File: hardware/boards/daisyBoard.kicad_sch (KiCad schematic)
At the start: 113 parts, among them IC1 TL072HIDR, IC2 TL072HIDR, IC3 TL072HIDR, IC4 TL072HIDR, J1 LEFT Pin ROW, J10 AudioJack_OUT_2, J11 AudioJack_OUT_2, J13 LEFT Pin ROW Daisy, J14 RIGHT Pin ROW DAISY, J15 Daisy Pin Breakout LEFT, J16 Daisy PIN Breakout RIGHT, J2 RIGHT Pin Row, J3 ESP32 Pin Breakout RIGHT, J4 ESP32 Pin Breakout LEFT, J6 AudioJack3, J7 AudioJack3, J8 AudioJack_IN_1, J9 AudioJack_IN_2, U1 MCP6002-xSN, U2 MCP6002-xSN, U3 MCP6002-xSN

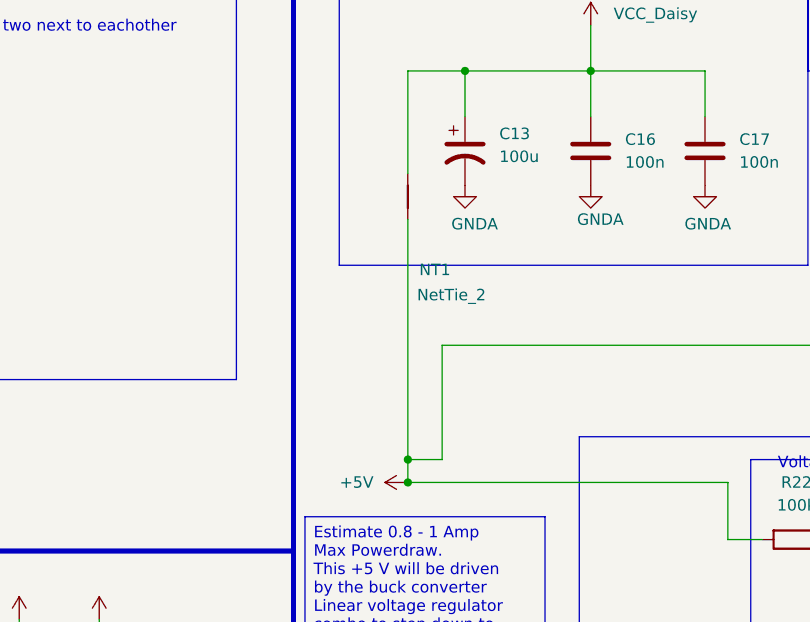
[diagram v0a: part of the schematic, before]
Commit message: moved some pads again
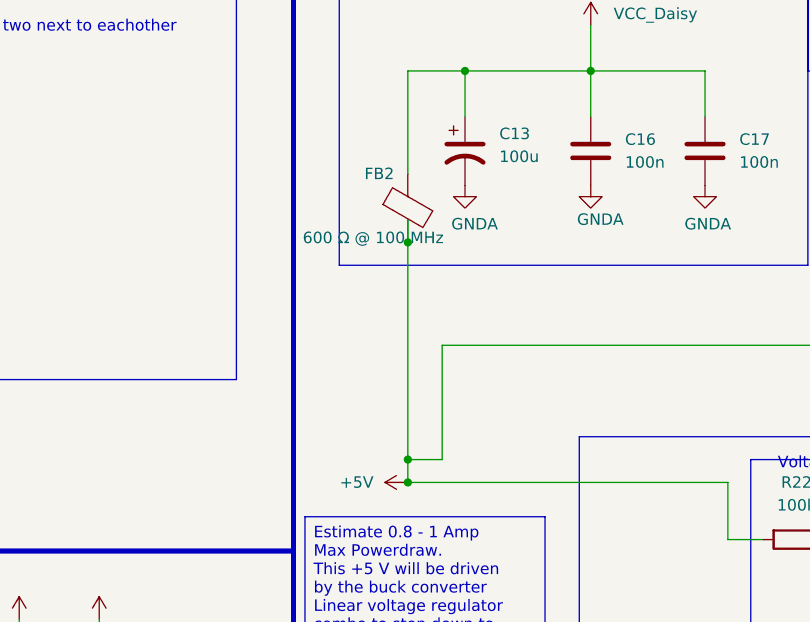
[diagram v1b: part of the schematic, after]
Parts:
- removed NT1: NetTie_2, NetTie:NetTie-2_SMD_Pad0.5mm, symbol Device:NetTie_2
- added FB2: 600 Ω @ 100 MHz, Inductor_SMD:L_0805_2012Metric, symbol Device:FerriteBead
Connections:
- net +5V: now also FB2.2
- net VCC_Daisy: now also FB2.1
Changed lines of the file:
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@@
 	)
 	(junction
+		(at 387.35 173.99)
+		(diameter 0)
+		(color 0 0 0 0)
+	)
+	(junction
 		(at 321.31 36.83)
 		(diameter 0)
@@
 	(wire
 		(pts
-			(xy 387.35 171.45) (xy 387.35 198.12)
+			(xy 387.35 171.45) (xy 387.35 173.99)
 		)
 		(stroke
@@
 	(wire
 		(pts
+			(xy 387.35 173.99) (xy 387.35 198.12)
+		)
+		(stroke
+			(width 0)
+			(type default)
+		)
+	)
+	(wire
+		(pts
 			(xy 307.34 238.76) (xy 307.34 254)
 		)
@@
 	)
 	(symbol
+		(lib_id "Device:FerriteBead")
+		(at 387.35 170.18 0)
+		(unit 1)
+		(body_style 1)
+		(exclude_from_sim no)
+		(in_bom yes)
+		(on_board yes)
+		(in_pos_files yes)
+		(dnp no)
+		(property "Reference" "FB2"
+			(at 382.524 166.37 0)
+			(show_name no)
+			(do_not_autoplace no)
+			(effects
+				(font
+					(size 1.27 1.27)
+				)
+				(justify left)
+			)
+		)
+		(property "Value" "600 Ω @ 100 MHz"
+			(at 375.666 173.482 0)
+			(show_name no)
+			(do_not_autoplace no)
+			(effects
+				(font
+					(size 1.27 1.27)
+				)
+				(justify left)
+			)
+		)
+		(property "Footprint" "Inductor_SMD:L_0805_2012Metric"
+			(at 385.572 170.18 90)
+			(hide yes)
+			(show_name no)
+			(do_not_autoplace no)
+			(effects
+				(font
+					(size 1.27 1.27)
+				)
+			)
+		)
+		(property "Datasheet" ""
+			(at 387.35 170.18 0)
+			(hide yes)
+			(show_name no)
+			(do_not_autoplace no)
+			(effects
+				(font
+					(size 1.27 1.27)
+				)
+			)
+		)
+		(property "Description" "Ferrite bead"
+			(at 387.35 170.18 0)
+			(hide yes)
+			(show_name no)
+			(do_not_autoplace no)
+			(effects
+				(font
+					(size 1.27 1.27)
+				)
+			)
+		)
+		(pin "2"
+		)
+		(pin "1"
+		)
+		(instances
+			(project "daisyBoard"
+				(path "/f52c2822-383d-4296-bc07-76547c2833aa"
+					(reference "FB2")
+					(unit 1)
+				)
+			)
+		)
+	)
+	(symbol
 		(lib_id "power:+3.3VA")
 		(at 48.26 139.7 270)
@@
 					(unit 1)
 				)
-			)
-		)
-	)
-	(symbol
-		(lib_id "Device:NetTie_2")
-		(at 387.35 168.91 90)
-		(unit 1)
-		(body_style 1)
-		(exclude_from_sim no)
-		(in_bom no)
-		(on_board yes)
-		(in_pos_files yes)
-		(dnp no)
-		(property "Reference" "NT1"
-			(at 388.62 177.038 90)
-			(show_name no)
-			(do_not_autoplace no)
-			(effects
-				(font
-					(size 1.27 1.27)
-				)
-				(justify right)
-			)
-		)
-		(property "Value" "NetTie_2"
-			(at 388.366 179.832 90)
-			(show_name no)
-			(do_not_autoplace no)
-			(effects
-				(font
-					(size 1.27 1.27)
-				)
-				(justify right)
-			)
-		)
-		(property "Footprint" "NetTie:NetTie-2_SMD_Pad0.5mm"
-			(at 387.35 168.91 0)
-			(hide yes)
-			(show_name no)
-			(do_not_autoplace no)
-			(effects
-				(font
-					(size 1.27 1.27)
-				)
-			)
-		)
-		(property "Datasheet" ""
-			(at 387.35 168.91 0)
-			(hide yes)
-			(show_name no)
-			(do_not_autoplace no)
-			(effects
-				(font
-					(size 1.27 1.27)
-				)
-			)
-		)
-		(property "Description" "Net tie, 2 pins"
-			(at 387.35 168.91 0)
-			(hide yes)
-			(show_name no)
-			(do_not_autoplace no)
-			(effects
-				(font
-					(size 1.27 1.27)
-				)
-			)
-		)
-		(pin "2"
-		)
-		(pin "1"
-		)
-		(instances
-			(project "daisyBoard"
-				(path "/f52c2822-383d-4296-bc07-76547c2833aa"
-					(reference "NT1")
-					(unit 1)
-				)

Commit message: did drc checks fix and connected flaoting pins on op amps
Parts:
- removed R24: 100R, Resistor_SMD:R_0805_2012Metric, symbol Device:R
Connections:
- net VREF: now also IC1.5 (+), IC2.5 (+), IC3.5 (+), IC4.5 (+), U3.1
- net at C15.1, C19.1, C20.1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: now also U3.5 (+)
- net at IC3.6 (-): now also IC3.7
- net at IC1.6 (-): now also IC1.7
- net at U3.6 (-): now also U3.7
- net at IC4.6 (-): now also IC4.7
- net at IC2.6 (-): now also IC2.7
- no-connect marks 25 -> 10
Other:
- note added: "Tie up floating pins"
- moved on the sheet: C29, FB2, U1C

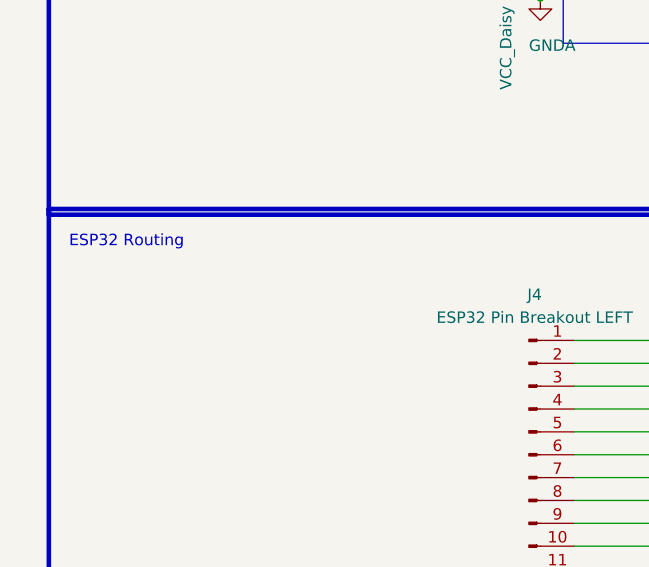
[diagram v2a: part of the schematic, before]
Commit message: updated some still in pad connections
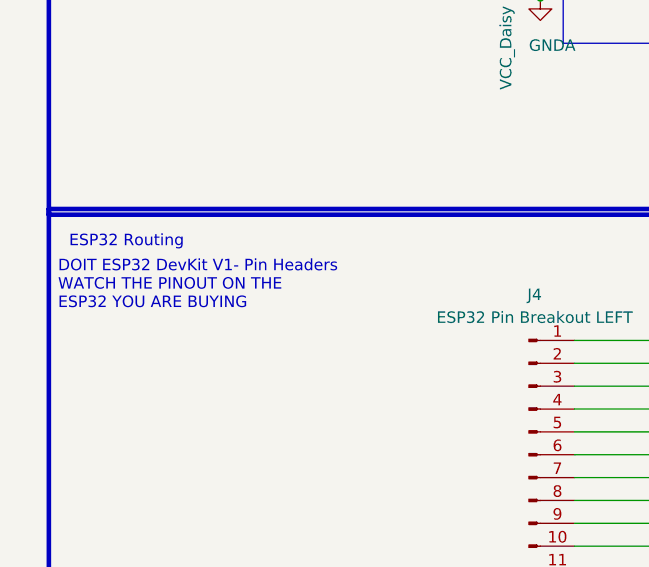
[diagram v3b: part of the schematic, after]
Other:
- note added: "DOIT ESP32 DevKit V1- Pin Headers WATCH THE PINOUT ON THE ESP32 YOU ARE BUYING"
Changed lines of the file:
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@@
+		)
+	)
+	(text "DOIT ESP32 DevKit V1- Pin Headers\nWATCH THE PINOUT ON THE \nESP32 YOU ARE BUYING"
+		(exclude_from_sim no)
+		(at 25.146 219.964 0)
+		(effects
+			(font
+				(size 1.27 1.27)
+			)
+			(justify left)
 		)
 	)

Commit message: last review and update of some things. Still need to adress VREF trace length
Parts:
- added R24: 100, Resistor_SMD:R_0805_2012Metric, symbol Device:R
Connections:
- net VREF: now also R24.2; no longer U3.1, U3.2 (-)
- new net: R24.1, U3.1, U3.2 (-)
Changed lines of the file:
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@@
 	)
 	(junction
-		(at 497.84 209.55)
-		(diameter 0)
-		(color 0 0 0 0)
-	)
-	(junction
 		(at 234.95 91.44)
 		(diameter 0)
@@
 	)
 	(junction
+		(at 497.84 209.55)
+		(diameter 0)
+		(color 0 0 0 0)
+	)
+	(junction
 		(at 252.73 91.44)
 		(diameter 0)
@@
 	(wire
 		(pts
-			(xy 497.84 209.55) (xy 505.46 209.55)
+			(xy 497.84 209.55) (xy 500.38 209.55)
 		)
 		(stroke
@@
 	(wire
 		(pts
+			(xy 508 209.55) (xy 509.27 209.55)
+		)
+		(stroke
+			(width 0)
+			(type default)
+		)
+	)
+	(wire
+		(pts
 			(xy 227.33 40.64) (xy 229.87 40.64)
 		)
@@
 	(symbol
 		(lib_id "power:+5V")
-		(at 505.46 209.55 270)
+		(at 509.27 209.55 270)
 		(unit 1)
 		(body_style 1)
@@
 		(in_pos_files yes)
 		(dnp no)
-		(fields_autoplaced yes)
 		(property "Reference" "#PWR043"
-			(at 501.65 209.55 0)
+			(at 505.46 209.55 0)
 			(hide yes)
 			(show_name no)
@@
 		)
 		(property "Value" "VREF"
-			(at 509.27 209.5499 90)
+			(at 510.032 207.01 90)
 			(show_name no)
 			(do_not_autoplace no)
@@
 		)
 		(property "Footprint" ""
-			(at 505.46 209.55 0)
+			(at 509.27 209.55 0)
 			(hide yes)
 			(show_name no)
@@
 		)
 		(property "Datasheet" ""
-			(at 505.46 209.55 0)
+			(at 509.27 209.55 0)
 			(hide yes)
 			(show_name no)
@@
 		)
 		(property "Description" "Power symbol creates a global label with name \"+5V\""
-			(at 505.46 209.55 0)
+			(at 509.27 209.55 0)
 			(hide yes)
 			(show_name no)
@@
 					(unit 1)
 				)
+			)
+		)
+	)
+	(symbol
+		(lib_id "Device:R")
+		(at 504.19 209.55 90)
+		(unit 1)
+		(body_style 1)
+		(exclude_from_sim no)
+		(in_bom yes)
+		(on_board yes)
+		(in_pos_files yes)
+		(dnp no)
+		(fields_autoplaced yes)
+		(property "Reference" "R24"
+			(at 504.19 203.2 90)
+			(show_name no)
+			(do_not_autoplace no)
+			(effects
+				(font
+					(size 1.27 1.27)
+				)
+			)
+		)
+		(property "Value" "100"
+			(at 504.19 205.74 90)
+			(show_name no)
+			(do_not_autoplace no)
+			(effects
+				(font
+					(size 1.27 1.27)
+				)
+			)
+		)
+		(property "Footprint" "Resistor_SMD:R_0805_2012Metric"
+			(at 504.19 211.328 90)
+			(hide yes)
+			(show_name no)
+			(do_not_autoplace no)
+			(effects
+				(font
+					(size 1.27 1.27)
+				)
+			)
+		)
+		(property "Datasheet" ""
+			(at 504.19 209.55 0)
+			(hide yes)
+			(show_name no)
+			(do_not_autoplace no)
+			(effects
+				(font
+					(size 1.27 1.27)
+				)
+			)
+		)
+		(property "Description" "Resistor"
+			(at 504.19 209.55 0)
+			(hide yes)
+			(show_name no)
+			(do_not_autoplace no)
+			(effects
+				(font
+					(size 1.27 1.27)
+				)
+			)
+		)
+		(pin "1"
+		)
+		(pin "2"
+		)
+		(instances
+			(project "daisyBoard"
+				(path "/f52c2822-383d-4296-bc07-76547c2833aa"
+					(reference "R24")
+					(unit 1)
+				)

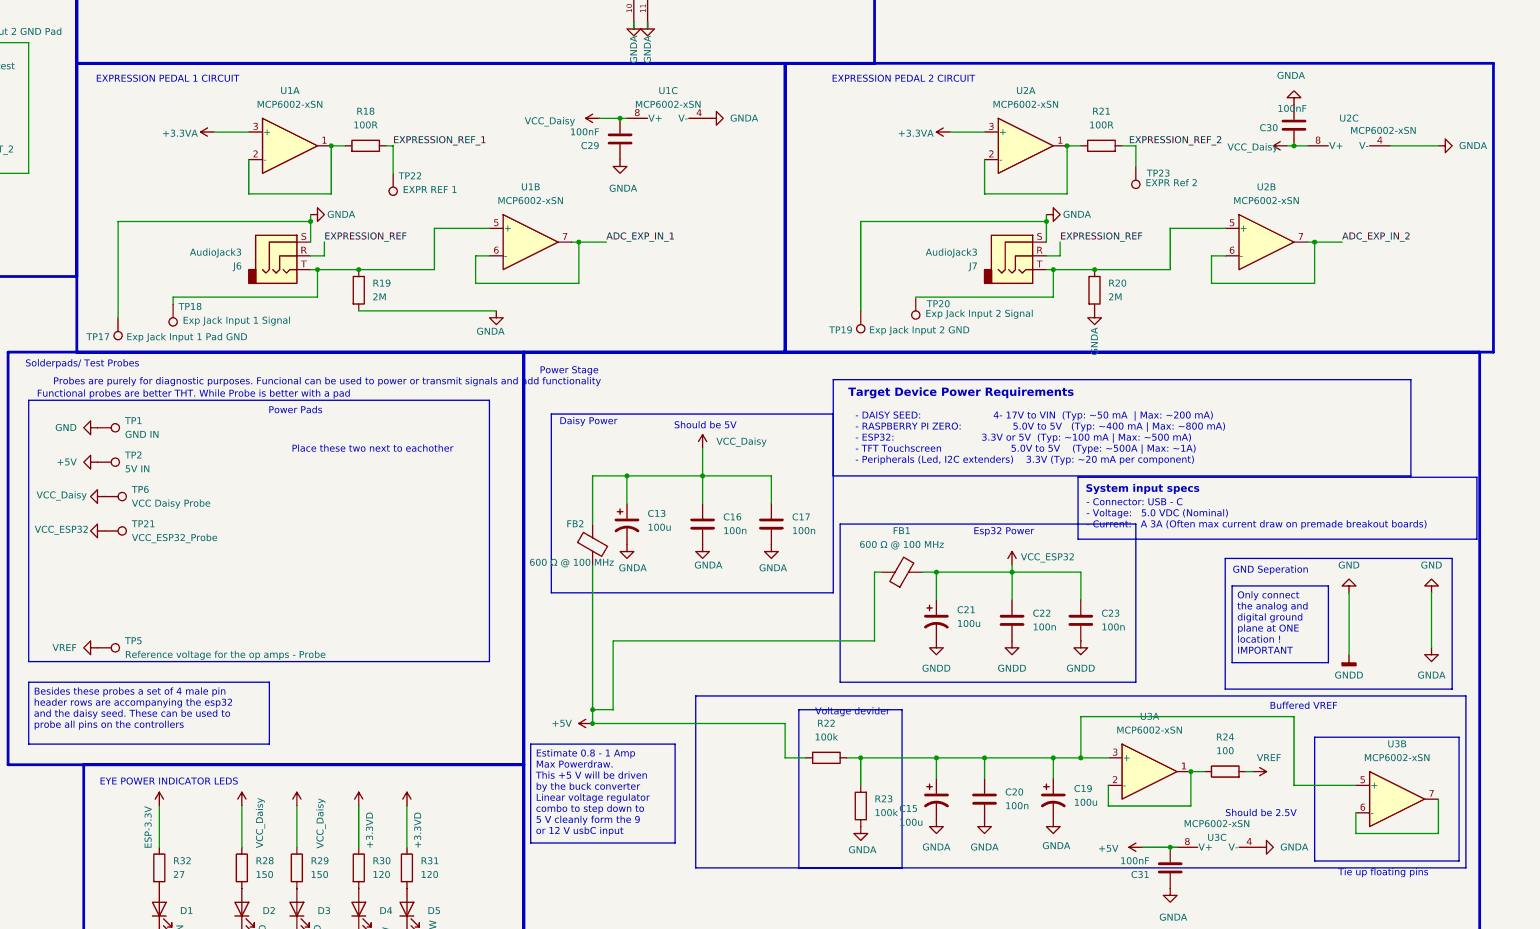
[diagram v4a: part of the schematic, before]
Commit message: Changed copper pours to exclude wide area around antenna
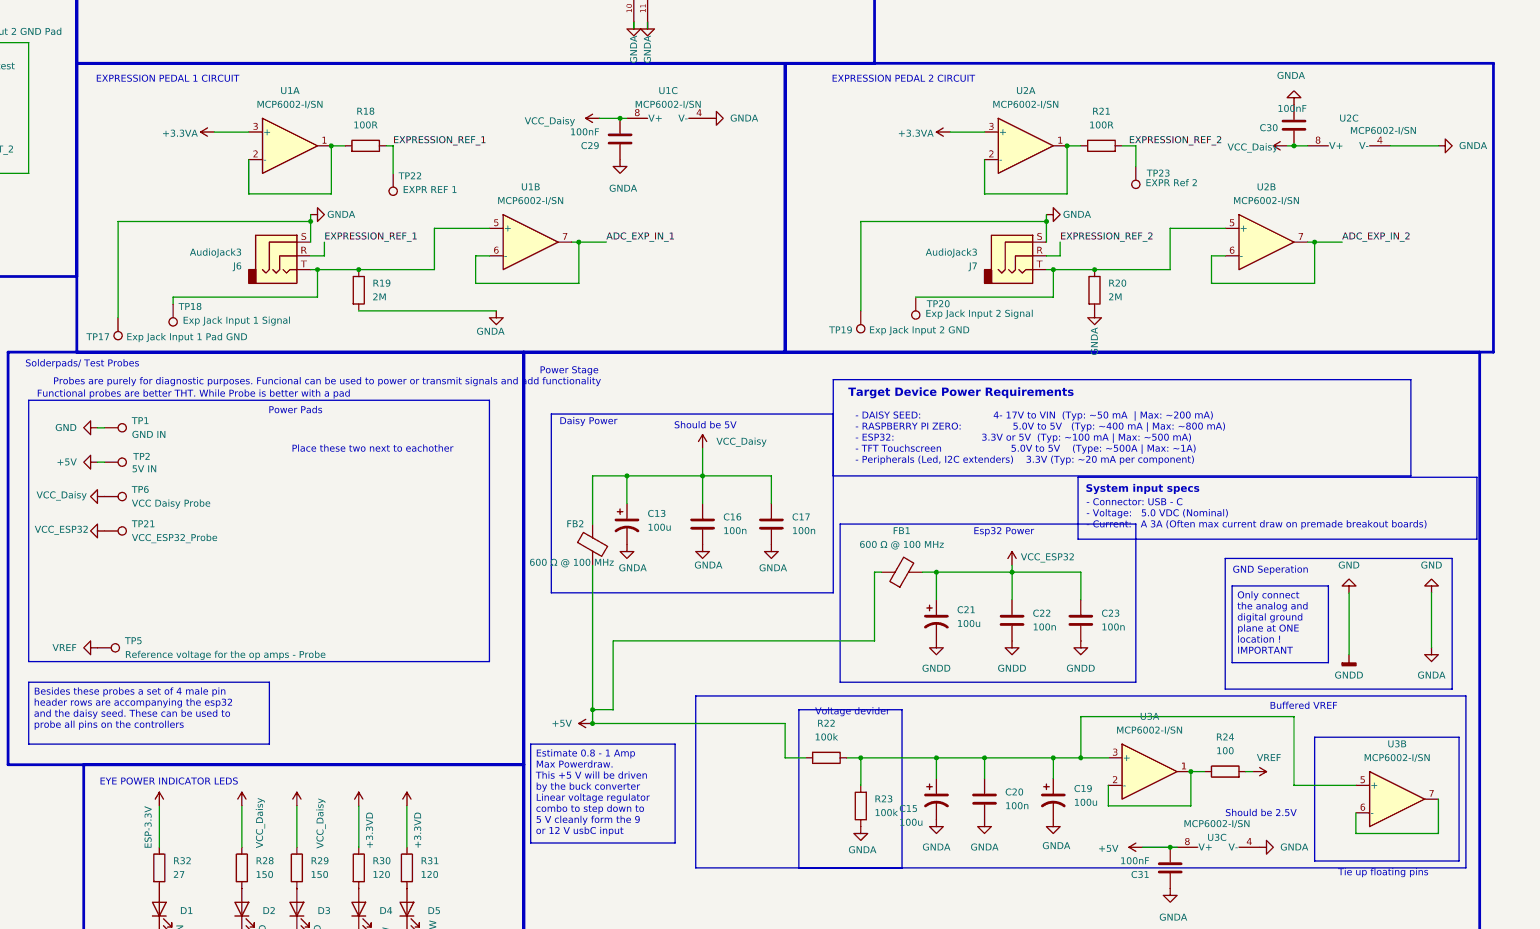
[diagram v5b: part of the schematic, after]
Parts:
- U1, U2, U3: value MCP6002-xSN -> MCP6002-I/SN
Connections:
- net EXPRESSION_REF_1: now also J6.R
- net EXPRESSION_REF_2: now also J7.R
- removed net EXPRESSION_REF: J6.R, J7.R
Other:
- moved on the sheet: TP1, TP2
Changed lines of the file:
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@@
 	(wire
 		(pts
+			(xy 297.18 152.4) (xy 295.91 152.4)
+		)
+		(stroke
+			(width 0)
+			(type default)
+		)
+	)
+	(wire
+		(pts
 			(xy 137.16 252.73) (xy 168.91 252.73)
 		)
@@
 	(wire
 		(pts
+			(xy 297.18 146.05) (xy 295.91 146.05)
+		)
+		(stroke
+			(width 0)
+			(type default)
+		)
+	)
+	(wire
+		(pts
 			(xy 166.37 38.1) (xy 170.18 38.1)
 		)
@@
 		)
 	)
-	(label "EXPRESSION_REF"
+	(label "EXPRESSION_REF_1"
 		(at 337.82 111.76 0)
 		(effects
@@
 		)
 	)
-	(label "EXPRESSION_REF"
+	(label "EXPRESSION_REF_2"
 		(at 473.71 111.76 0)
 		(effects
@@
 			)
 		)
-		(property "Value" "MCP6002-xSN"
+		(property "Value" "MCP6002-I/SN"
 			(at 490.22 201.93 0)
 			(show_name no)
@@
 			)
 		)
-		(property "Value" "MCP6002-xSN"
+		(property "Value" "MCP6002-I/SN"
 			(at 511.81 104.14 0)
 			(show_name no)
@@
 			)
 		)
-		(property "Value" "MCP6002-xSN"
+		(property "Value" "MCP6002-I/SN"
 			(at 401.32 86.36 90)
 			(show_name no)
@@
 			)
 		)
-		(property "Value" "MCP6002-xSN"
+		(property "Value" "MCP6002-I/SN"
 			(at 467.36 86.36 0)
 			(show_name no)
@@
 			)
 		)
-		(property "Value" "MCP6002-xSN"
+		(property "Value" "MCP6002-I/SN"
 			(at 502.666 219.202 90)
 			(show_name no)
@@
 	(symbol
 		(lib_id "Connector:TestPoint")
-		(at 295.91 152.4 270)
+		(at 297.18 152.4 270)
 		(unit 1)
 		(body_style 1)
@@
 		(in_pos_files yes)
 		(dnp no)
-		(fields_autoplaced yes)
 		(property "Reference" "TP2"
-			(at 300.99 151.1299 90)
+			(at 302.514 151.384 90)
 			(show_name no)
 			(do_not_autoplace no)
@@
 		)
 		(property "Value" "5V IN"
-			(at 300.99 153.6699 90)
+			(at 302.26 153.6699 90)
 			(show_name no)
 			(do_not_autoplace no)
@@
 		)
 		(property "Footprint" "TestPoint:TestPoint_THTPad_D2.5mm_Drill1.2mm"
-			(at 295.91 157.48 0)
+			(at 297.18 157.48 0)
 			(hide yes)
 			(show_name no)
@@
 		)
 		(property "Datasheet" ""
-			(at 295.91 157.48 0)
+			(at 297.18 157.48 0)
 			(hide yes)
 			(show_name no)
@@
 		)
 		(property "Description" "test point"
-			(at 295.91 152.4 0)
+			(at 297.18 152.4 0)
 			(hide yes)
 			(show_name no)
@@
 			)
 		)
-		(property "Value" "MCP6002-xSN"
+		(property "Value" "MCP6002-I/SN"
 			(at 375.92 104.14 0)
 			(show_name no)
@@
 			)
 		)
-		(property "Value" "MCP6002-xSN"
+		(property "Value" "MCP6002-I/SN"
 			(at 533.4 91.186 90)
 			(show_name no)
@@
 			)
 		)
-		(property "Value" "MCP6002-xSN"
+		(property "Value" "MCP6002-I/SN"
 			(at 535.94 207.01 0)
 			(show_name no)
@@
 	(symbol
 		(lib_id "Connector:TestPoint")
-		(at 295.91 146.05 270)
+		(at 297.18 146.05 270)
 		(unit 1)
 		(body_style 1)
@@
 		(fields_autoplaced yes)
 		(property "Reference" "TP1"
-			(at 300.99 144.7799 90)
+			(at 302.26 144.7799 90)
 			(show_name no)
 			(do_not_autoplace no)
@@
 		)
 		(property "Value" "GND IN"
-			(at 300.99 147.3199 90)
+			(at 302.26 147.3199 90)
 			(show_name no)
 			(do_not_autoplace no)
@@
 		)
 		(property "Footprint" "TestPoint:TestPoint_THTPad_D2.5mm_Drill1.2mm"
-			(at 295.91 151.13 0)
+			(at 297.18 151.13 0)
 			(hide yes)
 			(show_name no)
@@
 		)
 		(property "Datasheet" ""
-			(at 295.91 151.13 0)
+			(at 297.18 151.13 0)
 			(hide yes)
 			(show_name no)
@@
 		)
 		(property "Description" "test point"
-			(at 295.91 146.05 0)
+			(at 297.18 146.05 0)
 			(hide yes)
 			(show_name no)
@@
 			)
 		)
-		(property "Value" "MCP6002-xSN"
+		(property "Value" "MCP6002-I/SN"
 			(at 331.47 86.36 0)
 			(show_name no)

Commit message: fixed all DRC and ERC errors
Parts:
- removed C19: 100u, Capacitor_SMD:C_1206_3216Metric, symbol Device:C_Polarized_US
- C15: value 100u -> 10u
- R22, R23: value 100k -> 10k
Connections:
- net GND: now also C30.2; no longer C30.1
- net VCC_Daisy: now also C30.1; no longer C30.2
- no-connect marks 10 -> 9
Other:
- note added: "3V3"
- note added: "3v3A Daisy"
- note added: "3v3D Daisy"
- note added: "AGND Daisy"
- note added: "Audio In 1"
- note added: "Audio In 2"
- note added: "Audio Out 1"
- note added: "Audio Out 2"
- note added: "D0"
- note added: "D1"
- note added: "D10"
- note added: "D11"
- note added: "D12"
- note added: "D13"
- note added: "D13/Tx"
- note added: "D14"
- note added: "D14/Rx"
- note added: "D15"
- note added: "D16"
- note added: "D17"
- note added: "D18"
- note added: "D19"
- note added: "D2"
- note added: "D20"
- note added: "D21"
- note added: "D22"
- note added: "D23"
- note added: "D24"
- note added: "D25"
- note added: "D26"
- note added: "D27"
- note added: "D28"
- note added: "D29"
- note added: "D3"
- note added: "D30"
- note added: "D32"
- note added: "D33"
- note added: "D34"
- note added: "D35"
- note added: "D4"
- note added: "D5"
- note added: "D6"
- note added: "D7"
- note added: "D8"
- note added: "D9"
- note added: "DGND Daisy"
- note added: "EN"
- note added: "GND"
- note added: "RX0"
- note added: "TX0"
- note added: "VIN"
- note added: "VIN Daisy"
- note added: "VN"
- note added: "VP"
- note removed: "Place these two next to eachother"
- moved on the sheet: C15, C18, C20, C26, C30, IC1C, IC3C, TP1, TP2, TP21, TP5, TP6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
